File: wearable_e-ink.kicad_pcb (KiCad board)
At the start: 2 copper layers, 25 parts, among them U1 4*4*1_7, U10 NPN, U3 CH340C_USB, U5 ESP-12F(ESP8266MOD), U6 TYPE-C, U7 LDO, U8 4*4*1_7, U9 NPN

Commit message: First pcb design layout
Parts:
- moved C8 62.1 mm to (98.1, 30.4)
- moved R9 60.5 mm to (113.6, 25.2), turned to -90 degrees
- moved R8 56.4 mm to (111.2, 25.2), turned to -90 degrees
- moved R7 52.4 mm to (108.9, 25.2), turned to -90 degrees
- moved C6 48.3 mm to (98.7, 38.0), turned to -90 degrees
- moved R6 48.3 mm to (106.5, 25.2), turned to 90 degrees
- moved R13 46.5 mm to (93.9, 44.5), turned to -90 degrees
- moved C7 46.2 mm to (81.4, 42.1), turned to 90 degrees
- moved U3 45.6 mm to (92.3, 38.0)
- moved C4 45.2 mm to (81.4, 33.1), turned to -90 degrees
- moved U7 45.1 mm to (81.4, 37.6), turned to -90 degrees
- moved R5 44.3 mm to (104.2, 25.2), turned to 90 degrees
- moved U4 44.2 mm to (73.6, 34.2)
- moved C5 43.4 mm to (85.9, 38.0), turned to 90 degrees
- moved U6 41.5 mm to (92.1, 50.3)
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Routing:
- net /RST: track 0.00 -> 75.0 mm, vias 0 -> 2
- net /FLASH: track 0.00 -> 68.7 mm, vias 0 -> 2
- net /SCL: track 0.00 -> 53.9 mm, vias 0 -> 1
- net /D/C: track 0.00 -> 52.9 mm, vias 0 -> 1
- net /BUSY: track 0.00 -> 51.8 mm, vias 0 -> 1
- net /RES: track 0.00 -> 50.3 mm, vias 0 -> 1
- net /CS: track 0.00 -> 49.4 mm, vias 0 -> 1
- net /SDA: track 0.00 -> 39.3 mm
- net /LED: track 0.00 -> 37.1 mm
- net Net-(U5-GPIO15): track 0.00 -> 36.7 mm, vias 0 -> 2
- net /RXD: track 0.00 -> 34.1 mm, vias 0 -> 2
- net /TXD: track 0.00 -> 33.2 mm, vias 0 -> 2
- net GND: track 0.00 -> 27.2 mm, vias 0 -> 20
- net +3.3V: track 0.00 -> 20.8 mm, vias 0 -> 10
- net /RTS: track 0.00 -> 19.7 mm
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- added copper zone on In2.Cu, net +3.3V
- added copper zone on In2.Cu, net +5V
- added copper zone on B.Cu, net GND
- added copper zone on In1.Cu, net GND
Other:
- board outline added: 50.1 x 32.6 mm
- copper layers 2 -> 4
- board text added: "0.1uF"
- board text added: "10uF"
- board text added: "220R"
- board text added: "3.3V LDO"
- board text added: "5.1k"
- board text added: "5.1k x5"
- board text added: "CH340"
- board text added: "Display Bridge"
- board text added: "ESP-12F"
- board text added: "FLASH"
- board text added: "LED"
- board text added: "NPN x2"
- board text added: "RESET"
- board text added: "USB to UART"
- board text added: "USB-C"
- board text added: "pulldown/up network"

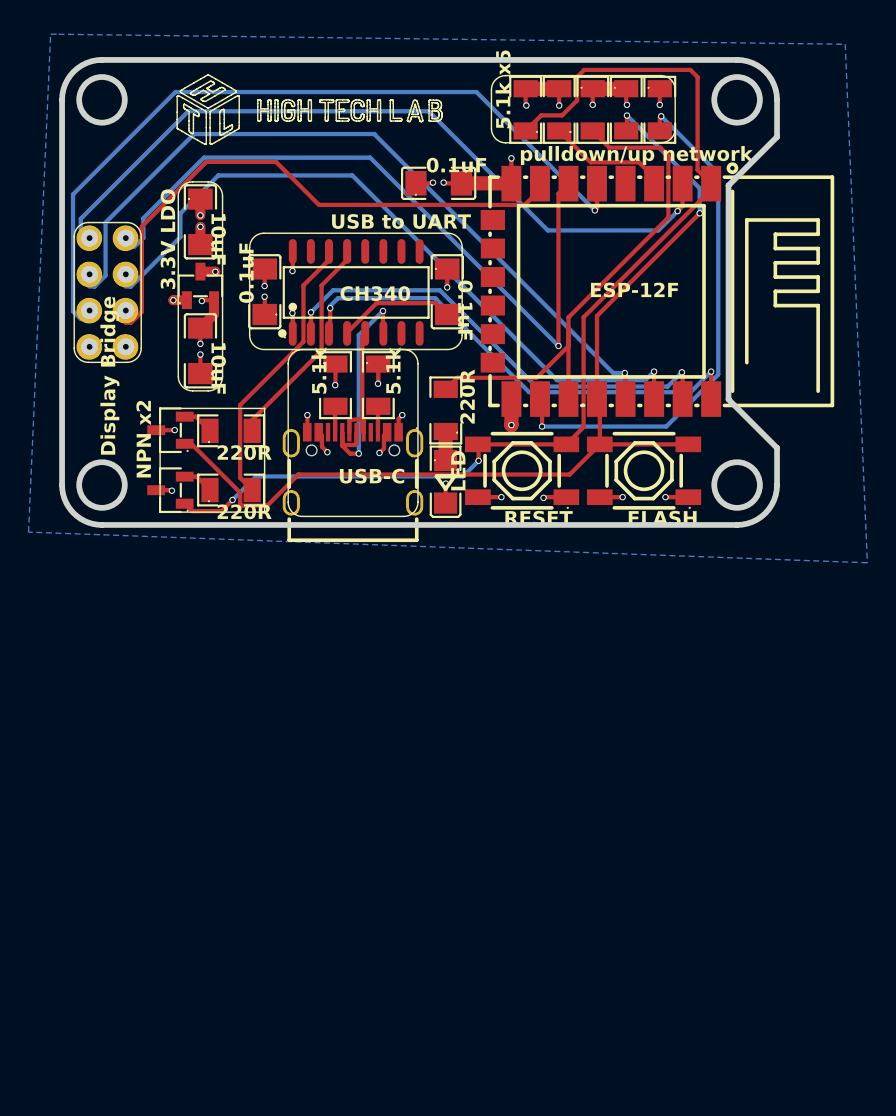
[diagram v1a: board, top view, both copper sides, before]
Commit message: Switched out daughter board for on-board FPC and display signal conditioning. First of V2
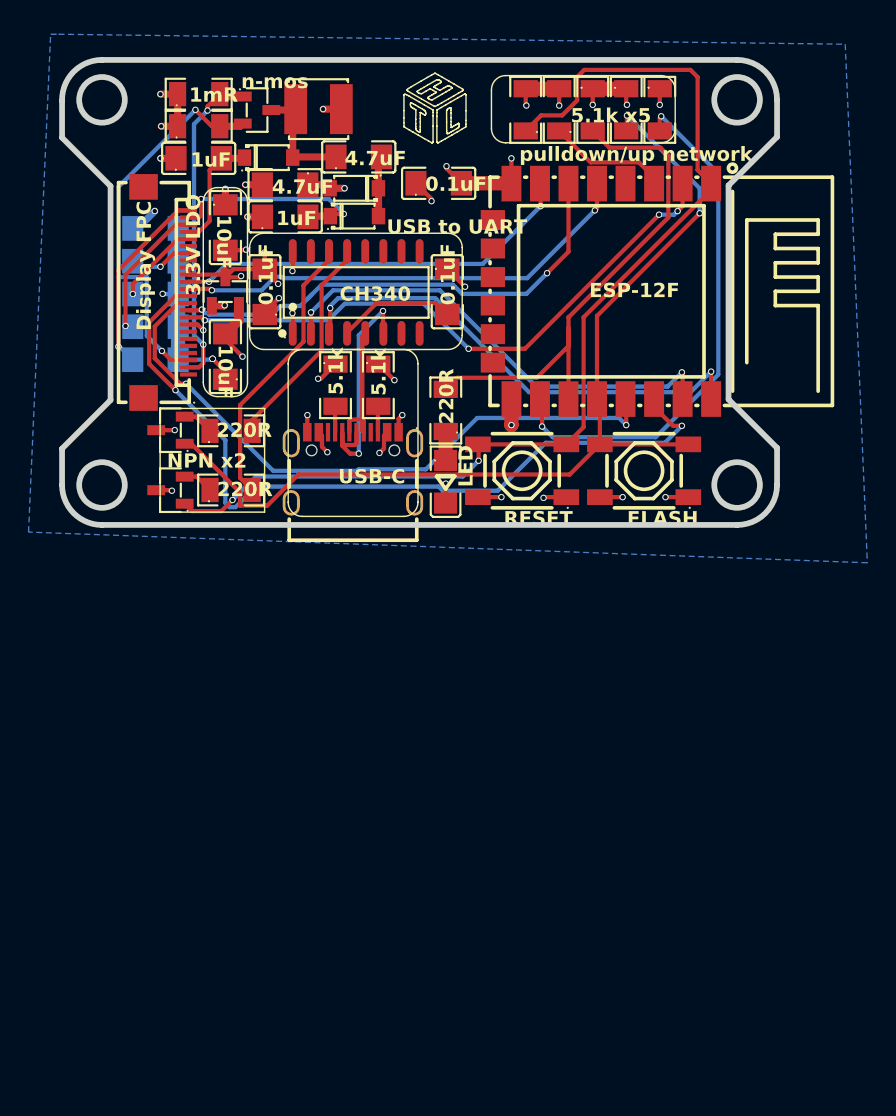
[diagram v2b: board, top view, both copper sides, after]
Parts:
- added C10: 1uF, wearable-e-inks:C1206, B.Cu at (78.2, 35.9)
- added C11: 1uF, wearable-e-inks:C1206, B.Cu at (78.2, 38.2)
- added C12: 1uF, wearable-e-inks:C1206, B.Cu at (78.2, 40.5)
- added C13: 1uF, wearable-e-inks:C1206, F.Cu at (87.3, 32.8)
- added C14: 1uF, wearable-e-inks:C1206, B.Cu at (78.2, 42.8)
- added C16: 4.7uF, wearable-e-inks:C1206, F.Cu at (87.3, 30.5)
- added C17: 4.7uF, wearable-e-inks:C1206, F.Cu at (92.5, 28.6)
- added C18: 1uF, wearable-e-inks:C1206, F.Cu at (81.3, 28.6)
- added C9: 1uF, wearable-e-inks:C1206, B.Cu at (78.2, 33.6)
- added D1: shottky, wearable-e-inks:SOD-123_L2.8-W1.8-LS3.7-RD, F.Cu at (86.2, 28.6)
- added D2: shottky, wearable-e-inks:SOD-123_L2.8-W1.8-LS3.7-RD, F.Cu at (92.2, 30.8)
- added D3: shottky, wearable-e-inks:SOD-123_L2.8-W1.8-LS3.7-RD, F.Cu at (92.2, 32.7)
- added L2: 47uF, wearable-e-inks:IND-SMD_L4.0-W4.0, F.Cu at (89.7, 25.2)
- added R14: 2.2R, wearable-e-inks:R1206, F.Cu at (81.3, 26.4)
- added R3: 1MR, wearable-e-inks:R1206, F.Cu at (81.3, 24.1)
- added U11: 05A20H24P, wearable-e-inks:FPC-SMD_24P-P0.50_05A20H24P, F.Cu at (79.0, 38.0)
- U4: value ~ -> N-MOS; footprint wearable-e-inks:8pinheader -> wearable-e-inks:SOT-23-LDO
- moved U4 14.8 mm to (85.4, 25.3), turned to 180 degrees
- moved U7 1.80 mm to (83.2, 38.0)
- moved C4 1.80 mm to (83.2, 33.5)
- moved C7 1.80 mm to (83.2, 42.5)
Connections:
- U4 pad 1: /BUSY -> /GDR
- U4 pad 2: /RES -> /RESE
- U4 pad 3: /D/C -> Net-(D1-A)
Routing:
- net /RESE: track 0.00 -> 27.5 mm, vias 0 -> 2
- net GND: track 27.2 -> 51.4 mm, vias 20 -> 27
- net /GDR: track 0.00 -> 22.7 mm, vias 0 -> 2
- net /SCL: track 53.9 -> 32.9 mm, vias 1 -> 2
- net /RES: track 50.3 -> 34.4 mm, vias 1 -> 2
- net /PREVGL: track 0.00 -> 15.1 mm, vias 0 -> 2
- net +3.3V: track 20.8 -> 35.4 mm, vias 10 -> 14
- net Net-(U11-VCOM): track 0.00 -> 13.4 mm, vias 0 -> 1
- net /SDA: track 39.3 -> 28.5 mm, vias 0 -> 2
- net /BUSY: track 51.8 -> 42.2 mm, vias 1 -> 4
- net Net-(U11-VSL): track 0.00 -> 9.46 mm, vias 0 -> 1
- net Net-(D1-A): track 0.00 -> 8.28 mm
- net /PREVGH: track 0.00 -> 8.17 mm
- net /D/C: track 52.9 -> 45.2 mm, vias 1 -> 2
- net /CS: track 49.4 -> 56.2 mm, vias 1 -> 2
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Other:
- outline, holes or cut-outs redrawn
- board text added: "1mR"
- board text added: "1uF"
- board text added: "1uF x5"
- board text added: "4.7uF"
- board text added: "Display FPC"
- board text added: "n-mos"
- board text removed: "Display Bridge"
